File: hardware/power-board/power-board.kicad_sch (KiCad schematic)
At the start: 25 parts, among them J1 SW_SPST, J2 Main Board, J3 DMX512 Out Jack, J4 DMX512, K1 SPST-NO, K2 SPST-NO, P1 IEC320-C14, P2 IEC320-C13, P3 IEC320-C13, U1 NUD3112DMT1G, U2 MAX3075E

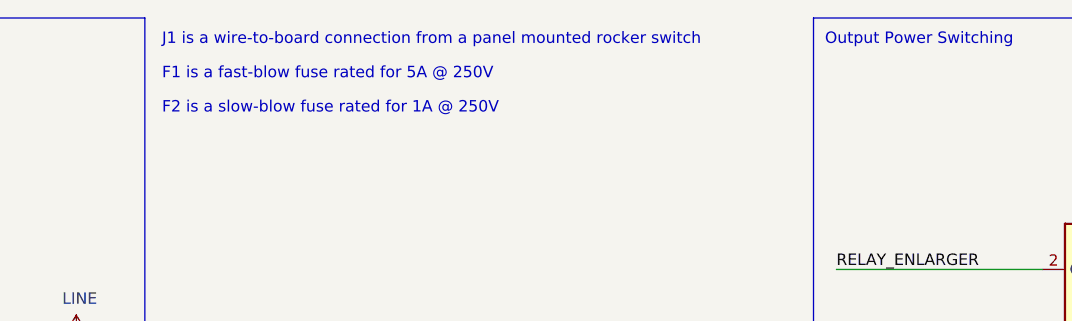
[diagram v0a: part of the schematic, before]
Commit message: Updated power switch connection and other layout adjustments
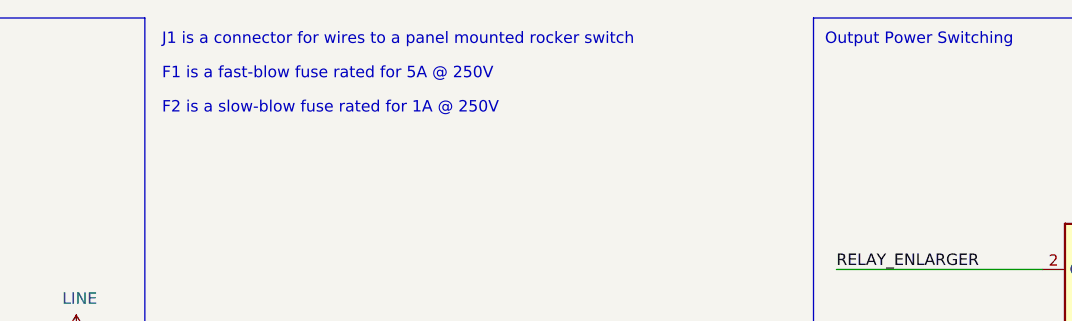
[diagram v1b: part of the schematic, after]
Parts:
- J1: footprint Connector_Wire:SolderWire-1.5sqmm_1x02_P7.8mm_D1.7mm_OD3.9mm -> lib_fp:TE_MATE-N-LOK_350428-x_1x02_P6.35mm_Vertical; Manufacturer (none) -> TE Connectivity; Manufacturer PN (none) -> 350428-1; Supplier (none) -> Digi-Key; Supplier PN (none) -> A1466-ND
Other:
- note added: "J1 is a connector for wires to a panel mounted rocker switch"
- note removed: "J1 is a wire-to-board connection from a panel mounted rocker switch"
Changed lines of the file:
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@@
     (effects (font (size 1.27 1.27)) (justify left bottom))
   )
-  (text "J1 is a wire-to-board connection from a panel mounted rocker switch"
+  (text "J1 is a connector for wires to a panel mounted rocker switch"
     (at 64.135 17.145 0)
     (effects (font (size 1.27 1.27)) (justify left bottom))
@@
       (effects (font (size 1.27 1.27)) hide)
     )
-    (property "Footprint" "Connector_Wire:SolderWire-1.5sqmm_1x02_P7.8mm_D1.7mm_OD3.9mm" (at 27.94 52.07 0)
-      (effects (font (size 1.27 1.27)) hide)
-    )
-    (property "Datasheet" "~" (at 27.94 52.07 0)
+    (property "Footprint" "lib_fp:TE_MATE-N-LOK_350428-x_1x02_P6.35mm_Vertical" (at 27.94 52.07 0)
+      (effects (font (size 1.27 1.27)) hide)
+    )
+    (property "Datasheet" "https://www.te.com/commerce/DocumentDelivery/DDEController?Action=srchrtrv&DocNm=350428&DocType=Customer+Drawing&DocLang=English" (at 27.94 52.07 0)
       (effects (font (size 1.27 1.27)) hide)
     )
@@
       (effects (font (size 1.27 1.27)))
     )
-    (pin "1")
+    (property "Description" "CONN HEADER VERT 2POS 6.35MM" (at 27.94 52.07 0)
+      (effects (font (size 1.27 1.27)) hide)
+    )
+    (property "Manufacturer" "TE Connectivity" (at 27.94 52.07 0)
+      (effects (font (size 1.27 1.27)) hide)
+    )
+    (property "Manufacturer PN" "350428-1" (at 27.94 52.07 0)
+      (effects (font (size 1.27 1.27)) hide)
+    )
+    (property "Supplier" "Digi-Key" (at 27.94 52.07 0)
+      (effects (font (size 1.27 1.27)) hide)
+    )
+    (property "Supplier PN" "A1466-ND" (at 27.94 52.07 0)
+      (effects (font (size 1.27 1.27)) hide)
+    )
+    (pin "1")

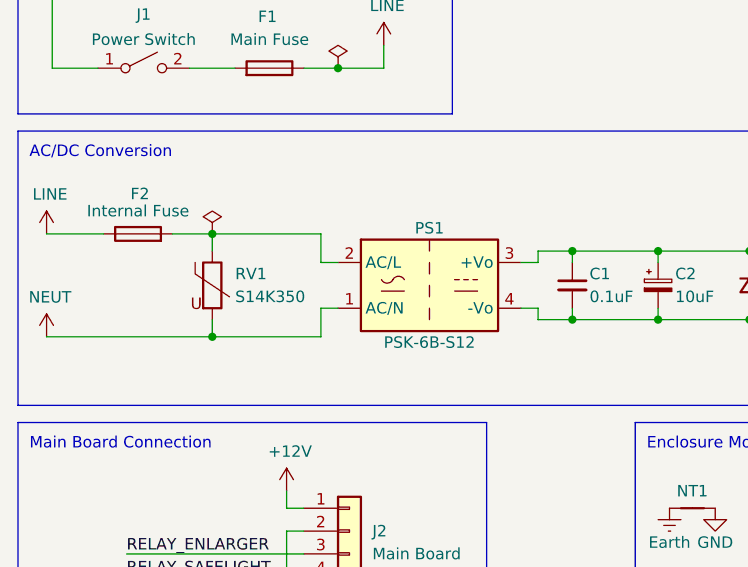
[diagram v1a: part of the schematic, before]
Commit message: Switched AC/DC converter from CUI to Cincon part
The new part has the same specifications, but is more available and
slightly lower cost. It also takes less board space, but specifies
clearance that cancels that out.
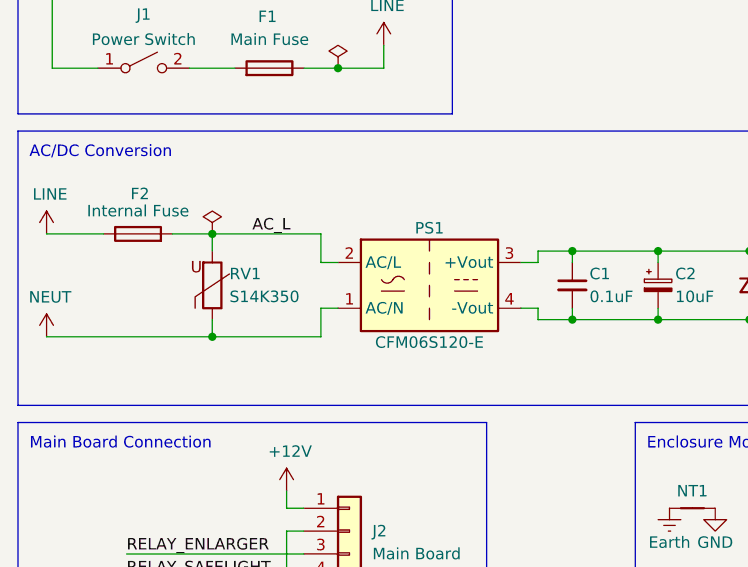
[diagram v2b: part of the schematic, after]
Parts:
- removed PS1: PSK-6B-S12, lib_fp:Converter_ACDC_CUI_PSK-6B, symbol Project:PSK-6B-S12
- added PS1: CFM06S120-E, lib_fp:Converter_ACDC_Cincom_CFM06Sxxx-E, symbol Project:CFM06S120-E
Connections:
- net +12V: now also PS1.3 (+Vout)
- net GND: now also PS1.4 (-Vout)
- net NEUT: now also RV1.1, PS1.1 (AC/N); no longer RV1.2
- net AC_L: now reaches F2.2
- net AC_L: now also RV1.2, PS1.2 (AC/L); no longer RV1.1
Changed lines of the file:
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@@
+    (effects (font (size 1.27 1.27)) (justify left bottom))
+  )
+  (label "AC_L" (at 40.005 70.485 0) (fields_autoplaced)
     (effects (font (size 1.27 1.27)) (justify left bottom))
   )
@@
         (path "/31a301d9-d769-4a35-943a-fe3e3609e773"
           (reference "H2") (unit 1)
+        )
+      )
+    )
+  )
+  (symbol (lib_id "Project:CFM06S120-E") (at 59.69 76.2 0) (unit 1)
+    (in_bom yes) (on_board yes) (dnp no)
+    (property "Reference" "PS1" (at 59.69 69.85 0)
+      (effects (font (size 1.27 1.27)))
+    )
+    (property "Value" "CFM06S120-E" (at 59.69 82.55 0)
+      (effects (font (size 1.27 1.27)))
+    )
+    (property "Footprint" "lib_fp:Converter_ACDC_Cincom_CFM06Sxxx-E" (at 59.69 85.09 0)
+      (effects (font (size 1.27 1.27)) hide)
+    )
+    (property "Datasheet" "https://www.cincon.com/productdownload/Datasheet-CFM06S-series.pdf" (at 59.69 86.995 0)
+      (effects (font (size 1.27 1.27)) hide)
+    )
+    (property "Description" "AC/DC CONVERTER 12V 6W" (at 59.69 76.2 0)
+      (effects (font (size 1.27 1.27)) hide)
+    )
+    (property "Manufacturer" "Cincon Electronics Co. LTD" (at 59.69 76.2 0)
+      (effects (font (size 1.27 1.27)) hide)
+    )
+    (property "Manufacturer PN" "CFM06S120-E" (at 59.69 76.2 0)
+      (effects (font (size 1.27 1.27)) hide)
+    )
+    (property "Supplier" "Digi-Key" (at 59.69 76.2 0)
+      (effects (font (size 1.27 1.27)) hide)
+    )
+    (property "Supplier PN" "2034-CFM06S120-E-ND" (at 59.69 76.2 0)
+      (effects (font (size 1.27 1.27)) hide)
+    )
+    (pin "1")
+    (pin "2")
+    (pin "3")
+    (pin "4")
+    (instances
+      (project "power-board"
+        (path "/31a301d9-d769-4a35-943a-fe3e3609e773"
+          (reference "PS1") (unit 1)
         )
       )
@@
     )
   )
-  (symbol (lib_id "Project:PSK-6B-S12") (at 59.69 76.2 0) (unit 1)
-    (in_bom yes) (on_board yes) (dnp no)
-    (property "Reference" "PS1" (at 59.69 69.85 0)
-      (effects (font (size 1.27 1.27)))
-    )
-    (property "Value" "PSK-6B-S12" (at 59.69 82.55 0)
-      (effects (font (size 1.27 1.27)))
-    )
-    (property "Footprint" "lib_fp:Converter_ACDC_CUI_PSK-6B" (at 59.69 85.09 0)
-      (effects (font (size 1.27 1.27)) hide)
-    )
-    (property "Datasheet" "https://www.cui.com/product/resource/psk-6b.pdf" (at 59.69 86.36 0)
-      (effects (font (size 1.27 1.27)) hide)
-    )
-    (property "Description" "AC/DC CONVERTER 12V 6W" (at 59.69 76.2 0)
-      (effects (font (size 1.27 1.27)) hide)
-    )
-    (property "Manufacturer" "CUI Inc." (at 59.69 76.2 0)
-      (effects (font (size 1.27 1.27)) hide)
-    )
-    (property "Manufacturer PN" "PSK-6B-S12" (at 59.69 76.2 0)
-      (effects (font (size 1.27 1.27)) hide)
-    )
-    (property "Supplier" "Digi-Key" (at 59.69 76.2 0)
-      (effects (font (size 1.27 1.27)) hide)
-    )
-    (property "Supplier PN" "102-4151-ND" (at 59.69 76.2 0)
-      (effects (font (size 1.27 1.27)) hide)
-    )
-    (pin "1")
-    (pin "2")
-    (pin "3")
-    (pin "4")
-    (instances
-      (project "power-board"
-        (path "/31a301d9-d769-4a35-943a-fe3e3609e773"
-          (reference "PS1") (unit 1)
-        )
-      )
-    )
-  )
-  (symbol (lib_id "Device:Varistor") (at 35.56 76.2 0) (unit 1)
-    (in_bom yes) (on_board yes) (dnp no)
-    (property "Reference" "RV1" (at 38.1 74.93 0)
-      (effects (font (size 1.27 1.27)) (justify left))
-    )
-    (property "Value" "S14K350" (at 38.1 77.47 0)
-      (effects (font (size 1.27 1.27)) (justify left))
-    )
+  (symbol (lib_id "Device:Varistor") (at 35.56 76.2 0) (mirror x) (unit 1)
+    (in_bom yes) (on_board yes) (dnp no)
+    (property "Reference" "RV1" (at 37.465 74.93 0)
+      (effects (font (size 1.27 1.27)) (justify left))
+    )
+    (property "Value" "S14K350" (at 37.465 77.47 0)
+      (effects (font (size 1.27 1.27)) (justify left))
+    )

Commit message: Changed IEC320 connectors on the power board
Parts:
- P1: footprint lib_fp:Bulgin_PX0580-PC -> lib_fp:Schurter_GSP1_9113_1; Manufacturer Bulgin -> Schurter; Manufacturer PN PX0580/PC -> GSP1.9113.1; Supplier PN 708-1341-ND -> 486-1008-ND
- P2, P3: footprint lib_fp:Bulgin_PX0675-PC -> lib_fp:Schurter_6182_0033; Manufacturer Bulgin -> Schurter; Manufacturer PN PX0675/PC -> 6182.0033; Supplier PN 708-1351-ND -> 486-1343-ND
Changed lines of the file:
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@@
       (effects (font (size 1.27 1.27)) (justify left))
     )
-    (property "Footprint" "lib_fp:Bulgin_PX0580-PC" (at 27.94 41.656 0)
-      (effects (font (size 1.27 1.27)) hide)
-    )
-    (property "Datasheet" "https://www.bulgin.com/products/pub/media/bulgin/data/IEC_connectors.pdf" (at 38.1 29.21 0)
+    (property "Footprint" "lib_fp:Schurter_GSP1_9113_1" (at 27.94 41.656 0)
+      (effects (font (size 1.27 1.27)) hide)
+    )
+    (property "Datasheet" "https://us.schurter.com/en/datasheet/typ_GSP1.pdf" (at 38.1 29.21 0)
       (effects (font (size 1.27 1.27)) hide)
     )
@@
       (effects (font (size 1.27 1.27)) hide)
     )
-    (property "Manufacturer" "Bulgin" (at 27.94 29.21 0)
-      (effects (font (size 1.27 1.27)) hide)
-    )
-    (property "Manufacturer PN" "PX0580/PC" (at 27.94 29.21 0)
+    (property "Manufacturer" "Schurter" (at 27.94 29.21 0)
+      (effects (font (size 1.27 1.27)) hide)
+    )
+    (property "Manufacturer PN" "GSP1.9113.1" (at 27.94 29.21 0)
       (effects (font (size 1.27 1.27)) hide)
     )
@@
       (effects (font (size 1.27 1.27)) hide)
     )
-    (property "Supplier PN" "708-1341-ND" (at 27.94 29.21 0)
+    (property "Supplier PN" "486-1008-ND" (at 27.94 29.21 0)
       (effects (font (size 1.27 1.27)) hide)
     )
@@
       (effects (font (size 1.27 1.27)) (justify left))
     )
-    (property "Footprint" "lib_fp:Bulgin_PX0675-PC" (at 243.205 75.946 0)
-      (effects (font (size 1.27 1.27)) hide)
-    )
-    (property "Datasheet" "https://www.bulgin.com/products/pub/media/bulgin/data/IEC_connectors.pdf" (at 253.365 63.5 0)
+    (property "Footprint" "lib_fp:Schurter_6182_0033" (at 243.205 75.946 0)
+      (effects (font (size 1.27 1.27)) hide)
+    )
+    (property "Datasheet" "https://us.schurter.com/bundles/snceschurter/epim/_ProdPool_/newDS/en/typ_5001.pdf" (at 253.365 63.5 0)
       (effects (font (size 1.27 1.27)) hide)
     )
@@
       (effects (font (size 1.27 1.27)) hide)
     )
-    (property "Manufacturer" "Bulgin" (at 243.205 63.5 0)
-      (effects (font (size 1.27 1.27)) hide)
-    )
-    (property "Manufacturer PN" "PX0675/PC" (at 243.205 63.5 0)
+    (property "Manufacturer" "Schurter" (at 243.205 63.5 0)
+      (effects (font (size 1.27 1.27)) hide)
+    )
+    (property "Manufacturer PN" "6182.0033" (at 243.205 63.5 0)
       (effects (font (size 1.27 1.27)) hide)
     )
@@
       (effects (font (size 1.27 1.27)) hide)
     )
-    (property "Supplier PN" "708-1351-ND" (at 243.205 63.5 0)
+    (property "Supplier PN" "486-1343-ND" (at 243.205 63.5 0)
       (effects (font (size 1.27 1.27)) hide)
     )
@@
       (effects (font (size 1.27 1.27)) (justify left))
     )
-    (property "Footprint" "lib_fp:Bulgin_PX0675-PC" (at 243.205 42.926 0)
-      (effects (font (size 1.27 1.27)) hide)
-    )
-    (property "Datasheet" "https://www.bulgin.com/products/pub/media/bulgin/data/IEC_connectors.pdf" (at 253.365 30.48 0)
+    (property "Footprint" "lib_fp:Schurter_6182_0033" (at 243.205 42.926 0)
+      (effects (font (size 1.27 1.27)) hide)
+    )
+    (property "Datasheet" "https://us.schurter.com/bundles/snceschurter/epim/_ProdPool_/newDS/en/typ_5001.pdf" (at 253.365 30.48 0)
       (effects (font (size 1.27 1.27)) hide)
     )
@@
       (effects (font (size 1.27 1.27)) hide)
     )
-    (property "Manufacturer" "Bulgin" (at 243.205 30.48 0)
-      (effects (font (size 1.27 1.27)) hide)
-    )
-    (property "Manufacturer PN" "PX0675/PC" (at 243.205 30.48 0)
+    (property "Manufacturer" "Schurter" (at 243.205 30.48 0)
+      (effects (font (size 1.27 1.27)) hide)
+    )
+    (property "Manufacturer PN" "6182.0033" (at 243.205 30.48 0)
       (effects (font (size 1.27 1.27)) hide)
     )
@@
       (effects (font (size 1.27 1.27)) hide)
     )
-    (property "Supplier PN" "708-1351-ND" (at 243.205 30.48 0)
-      (effects (font (size 1.27 1.27)) hide)
-    )
+    (property "Supplier PN" "486-1343-ND" (at 243.205 30.48 0)
+      (effects (font (size 1.27 1.27)) hide)
+    )
